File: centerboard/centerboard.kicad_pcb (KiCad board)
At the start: 2 copper layers, 71 parts, among them U1 ATmega32U4-A

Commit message: centerboard messing around
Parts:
- removed D1, D10, D11, D12, D13, D14, D15, D16, D17, D18, D19, D2, D20, D21, D22, D23, D24, D25, D26, D27, D28, D29, D3, D30, D31, D32, D33, D34, D35, D36, D37, D38, D39, D4, D40, D41, D42, D43, D44, D45, D46, D47, D48, D49, D5, D50, D51, D52, D53, D54, D55, D56, D6, D7, D8, D9: 1N4148W, Diode_SMD:D_SOD-123
- removed JC_LA1, JC_LB1, JC_LC1, JC_LD1, JC_LE1, JC_LF1, JC_LT1, JC_RA1, JC_RB1, JC_RC1, JC_RD1, JC_RE1, JC_RF1, JC_RT1: Conn_01x05_MountingPin, Connector_FFC-FPC:TE_84952-5_1x05-1MP_P1.0mm_Horizontal
- added J1: Conn_02x05_Odd_Even, Connector_IDC:IDC-Header_2x05_P2.54mm_Vertical, F.Cu at (96.5, 137.5)
- added J2: USB_B_Micro, Connector_USB:USB_Micro-B_Molex-105017-0001, F.Cu at (101.7, 49.5)
- added JC_L1: Conn_01x05_MountingPin, Connector_FFC-FPC:TE_84952-5_1x05-1MP_P1.0mm_Horizontal, F.Cu at (114.0, 82.2)
- added JC_L2: Conn_01x05_MountingPin, Connector_FFC-FPC:TE_84952-5_1x05-1MP_P1.0mm_Horizontal, F.Cu at (125.8, 85.0)
- added JC_L3: Conn_01x05_MountingPin, Connector_FFC-FPC:TE_84952-5_1x05-1MP_P1.0mm_Horizontal, F.Cu at (125.8, 101.0)
- added JC_L4: Conn_01x05_MountingPin, Connector_FFC-FPC:TE_84952-5_1x05-1MP_P1.0mm_Horizontal, F.Cu at (125.8, 117.0)
- added JC_L5: Conn_01x05_MountingPin, Connector_FFC-FPC:TE_84952-5_1x05-1MP_P1.0mm_Horizontal, F.Cu at (125.8, 133.0)
- added JC_L6: Conn_01x05_MountingPin, Connector_FFC-FPC:TE_84952-5_1x05-1MP_P1.0mm_Horizontal, F.Cu at (125.8, 149.0)
- added JC_L7: Conn_01x05_MountingPin, Connector_FFC-FPC:TE_84952-5_1x05-1MP_P1.0mm_Horizontal, F.Cu at (114.0, 151.8)
- added JC_R1: Conn_01x05_MountingPin, Connector_FFC-FPC:TE_84952-5_1x05-1MP_P1.0mm_Horizontal, F.Cu at (88.0, 82.2)
- added JC_R2: Conn_01x05_MountingPin, Connector_FFC-FPC:TE_84952-5_1x05-1MP_P1.0mm_Horizontal, F.Cu at (76.2, 85.0)
- added JC_R3: Conn_01x05_MountingPin, Connector_FFC-FPC:TE_84952-5_1x05-1MP_P1.0mm_Horizontal, F.Cu at (76.2, 101.0)
- added JC_R4: Conn_01x05_MountingPin, Connector_FFC-FPC:TE_84952-5_1x05-1MP_P1.0mm_Horizontal, F.Cu at (76.2, 117.0)
- added JC_R5: Conn_01x05_MountingPin, Connector_FFC-FPC:TE_84952-5_1x05-1MP_P1.0mm_Horizontal, F.Cu at (76.2, 133.0)
- added JC_R6: Conn_01x05_MountingPin, Connector_FFC-FPC:TE_84952-5_1x05-1MP_P1.0mm_Horizontal, F.Cu at (76.2, 149.0)
- added JC_R7: Conn_01x05_MountingPin, Connector_FFC-FPC:TE_84952-5_1x05-1MP_P1.0mm_Horizontal, F.Cu at (88.0, 151.8)
- added SW1: SW_Push, Button_Switch_SMD:SW_Push_SPST_NO_Alps_SKRK, F.Cu at (106.1, 133.0)
- moved U1 47.8 mm to (102.0, 103.0)
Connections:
- net Net-(U1-GND-Pad15) renamed GND
- net Net-(U1-VCC-Pad14) renamed VCC
- U1 pad 10: COL_RC -> MOSI
- U1 pad 11: COL_RD -> MISO
- U1 pad 12: COL_LA -> unconnected-(U1-PB7-Pad12)
- U1 pad 13: unconnected-(U1-~{RESET}-Pad13) -> RST
- U1 pad 18: COL_LD -> unconnected-(U1-PD0-Pad18)
- U1 pad 19: COL_LE -> unconnected-(U1-PD1-Pad19)
- U1 pad 20: COL_LF -> unconnected-(U1-PD2-Pad20)
- U1 pad 21: COL_LT -> unconnected-(U1-PD3-Pad21)
- U1 pad 22: ROW_2 -> unconnected-(U1-PD5-Pad22)
- U1 pad 25: ROW_1 -> unconnected-(U1-PD4-Pad25)
- U1 pad 26: ROW_3 -> unconnected-(U1-PD6-Pad26)
- U1 pad 27: ROW_4 -> unconnected-(U1-PD7-Pad27)
- U1 pad 28: COL_RE -> unconnected-(U1-PB4-Pad28)
- U1 pad 29: COL_RF -> unconnected-(U1-PB5-Pad29)
- U1 pad 3: unconnected-(U1-D--Pad3) -> Net-(J2-D-)
- U1 pad 30: COL_RT -> unconnected-(U1-PB6-Pad30)
- U1 pad 31: COL_LB -> unconnected-(U1-PC6-Pad31)
- U1 pad 32: COL_LC -> unconnected-(U1-PC7-Pad32)
- U1 pad 4: unconnected-(U1-D+-Pad4) -> Net-(J2-D+)
- U1 pad 8: COL_RA -> unconnected-(U1-PB0-Pad8)
- U1 pad 9: COL_RB -> SCK

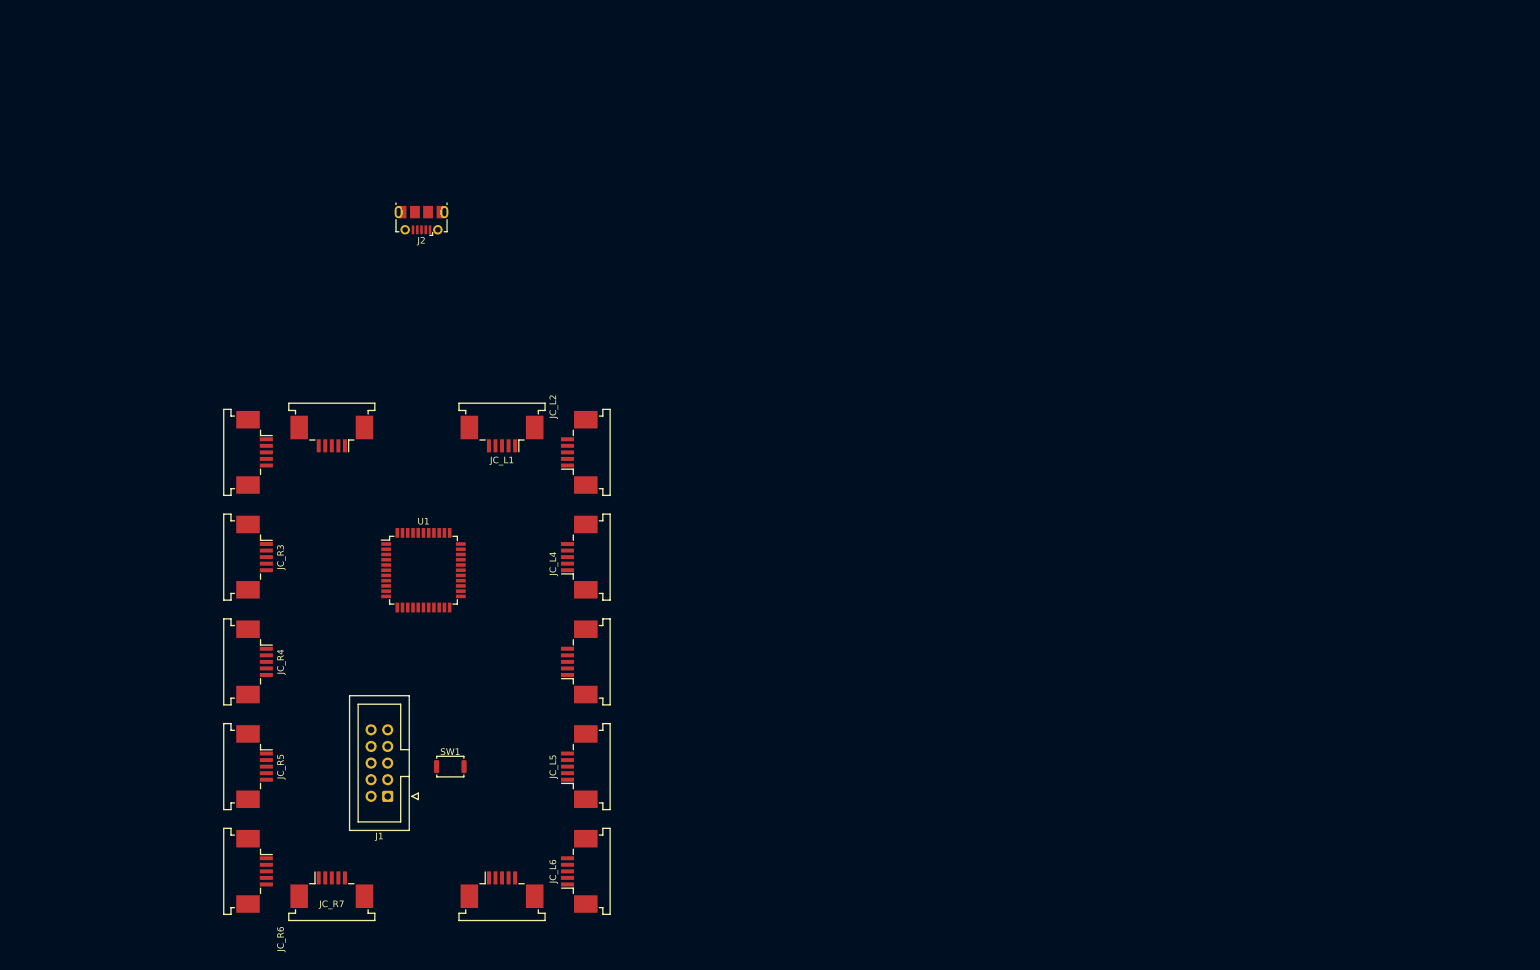
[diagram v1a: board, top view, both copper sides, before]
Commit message: Various tweaks. About to flip centerboard, not feeling too confident in the results there
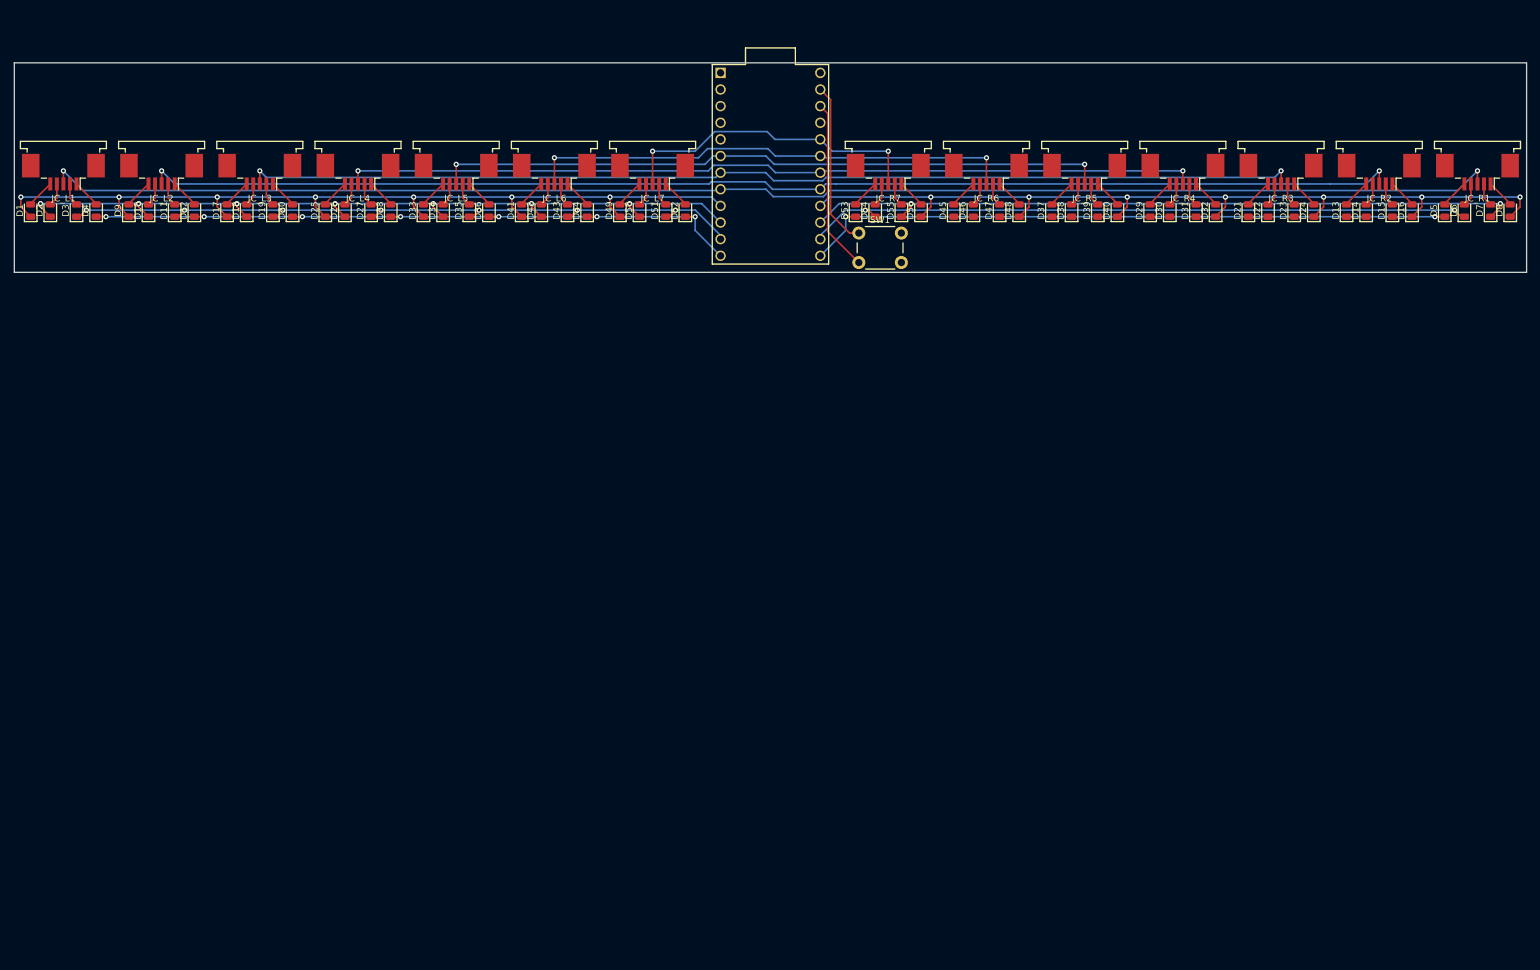
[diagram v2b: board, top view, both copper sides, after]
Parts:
- removed J1: Conn_02x05_Odd_Even, Connector_IDC:IDC-Header_2x05_P2.54mm_Vertical
- removed J2: USB_B_Micro, Connector_USB:USB_Micro-B_Molex-105017-0001
- added D1: 1N4148W, Diode_SMD:D_0805_2012Metric, F.Cu at (42.0, 48.1)
- added D10: 1N4148W, Diode_SMD:D_0805_2012Metric, F.Cu at (60.0, 48.1)
- added D11: 1N4148W, Diode_SMD:D_0805_2012Metric, F.Cu at (64.0, 48.1)
- added D12: 1N4148W, Diode_SMD:D_0805_2012Metric, F.Cu at (67.0, 48.1)
- added D13: 1N4148W, Diode_SMD:D_0805_2012Metric, F.Cu at (243.0, 48.1)
- added D14: 1N4148W, Diode_SMD:D_0805_2012Metric, F.Cu at (246.0, 48.1)
- added D15: 1N4148W, Diode_SMD:D_0805_2012Metric, F.Cu at (250.0, 48.1)
- added D16: 1N4148W, Diode_SMD:D_0805_2012Metric, F.Cu at (253.0, 48.1)
- added D17: 1N4148W, Diode_SMD:D_0805_2012Metric, F.Cu at (72.0, 48.1)
- added D18: 1N4148W, Diode_SMD:D_0805_2012Metric, F.Cu at (75.0, 48.1)
- added D19: 1N4148W, Diode_SMD:D_0805_2012Metric, F.Cu at (79.0, 48.1)
- added D2: 1N4148W, Diode_SMD:D_0805_2012Metric, F.Cu at (45.0, 48.1)
- added D20: 1N4148W, Diode_SMD:D_0805_2012Metric, F.Cu at (82.0, 48.1)
- added D21: 1N4148W, Diode_SMD:D_0805_2012Metric, F.Cu at (228.0, 48.1)
- added D22: 1N4148W, Diode_SMD:D_0805_2012Metric, F.Cu at (231.0, 48.1)
- added D23: 1N4148W, Diode_SMD:D_0805_2012Metric, F.Cu at (235.0, 48.1)
- added D24: 1N4148W, Diode_SMD:D_0805_2012Metric, F.Cu at (238.0, 48.1)
- added D25: 1N4148W, Diode_SMD:D_0805_2012Metric, F.Cu at (87.0, 48.1)
- added D26: 1N4148W, Diode_SMD:D_0805_2012Metric, F.Cu at (90.0, 48.1)
- added D27: 1N4148W, Diode_SMD:D_0805_2012Metric, F.Cu at (94.0, 48.1)
- added D28: 1N4148W, Diode_SMD:D_0805_2012Metric, F.Cu at (97.0, 48.1)
- added D29: 1N4148W, Diode_SMD:D_0805_2012Metric, F.Cu at (213.0, 48.1)
- added D3: 1N4148W, Diode_SMD:D_0805_2012Metric, F.Cu at (49.0, 48.1)
- added D30: 1N4148W, Diode_SMD:D_0805_2012Metric, F.Cu at (216.0, 48.1)
- added D31: 1N4148W, Diode_SMD:D_0805_2012Metric, F.Cu at (220.0, 48.1)
- added D32: 1N4148W, Diode_SMD:D_0805_2012Metric, F.Cu at (223.0, 48.1)
- added D33: 1N4148W, Diode_SMD:D_0805_2012Metric, F.Cu at (102.0, 48.1)
- added D34: 1N4148W, Diode_SMD:D_0805_2012Metric, F.Cu at (105.0, 48.1)
- added D35: 1N4148W, Diode_SMD:D_0805_2012Metric, F.Cu at (109.0, 48.1)
- added D36: 1N4148W, Diode_SMD:D_0805_2012Metric, F.Cu at (112.0, 48.1)
- added D37: 1N4148W, Diode_SMD:D_0805_2012Metric, F.Cu at (198.0, 48.1)
- added D38: 1N4148W, Diode_SMD:D_0805_2012Metric, F.Cu at (201.0, 48.1)
- added D39: 1N4148W, Diode_SMD:D_0805_2012Metric, F.Cu at (205.0, 48.1)
- added D4: 1N4148W, Diode_SMD:D_0805_2012Metric, F.Cu at (52.0, 48.1)
- added D40: 1N4148W, Diode_SMD:D_0805_2012Metric, F.Cu at (208.0, 48.1)
- added D41: 1N4148W, Diode_SMD:D_0805_2012Metric, F.Cu at (117.0, 48.1)
- added D42: 1N4148W, Diode_SMD:D_0805_2012Metric, F.Cu at (120.0, 48.1)
- added D43: 1N4148W, Diode_SMD:D_0805_2012Metric, F.Cu at (124.0, 48.1)
- added D44: 1N4148W, Diode_SMD:D_0805_2012Metric, F.Cu at (127.0, 48.1)
- added D45: 1N4148W, Diode_SMD:D_0805_2012Metric, F.Cu at (183.0, 48.1)
- added D46: 1N4148W, Diode_SMD:D_0805_2012Metric, F.Cu at (186.0, 48.1)
- added D47: 1N4148W, Diode_SMD:D_0805_2012Metric, F.Cu at (190.0, 48.1)
- added D48: 1N4148W, Diode_SMD:D_0805_2012Metric, F.Cu at (193.0, 48.1)
- added D49: 1N4148W, Diode_SMD:D_0805_2012Metric, F.Cu at (132.0, 48.1)
- added D5: 1N4148W, Diode_SMD:D_0805_2012Metric, F.Cu at (258.0, 48.1)
- added D50: 1N4148W, Diode_SMD:D_0805_2012Metric, F.Cu at (135.0, 48.1)
- added D51: 1N4148W, Diode_SMD:D_0805_2012Metric, F.Cu at (139.0, 48.1)
- added D52: 1N4148W, Diode_SMD:D_0805_2012Metric, F.Cu at (142.0, 48.1)
- added D53: 1N4148W, Diode_SMD:D_0805_2012Metric, F.Cu at (168.0, 48.1)
- added D54: 1N4148W, Diode_SMD:D_0805_2012Metric, F.Cu at (171.0, 48.1)
- added D55: 1N4148W, Diode_SMD:D_0805_2012Metric, F.Cu at (175.0, 48.1)
- added D56: 1N4148W, Diode_SMD:D_0805_2012Metric, F.Cu at (178.0, 48.1)
- added D6: 1N4148W, Diode_SMD:D_0805_2012Metric, F.Cu at (261.0, 48.1)
- added D7: 1N4148W, Diode_SMD:D_0805_2012Metric, F.Cu at (265.0, 48.1)
- added D8: 1N4148W, Diode_SMD:D_0805_2012Metric, F.Cu at (268.0, 48.1)
- added D9: 1N4148W, Diode_SMD:D_0805_2012Metric, F.Cu at (57.0, 48.1)
- SW1: footprint Button_Switch_SMD:SW_Push_SPST_NO_Alps_SKRK -> Button_Switch_THT:SW_PUSH_6mm
- U1: value ATmega32U4-A -> ProMicro; footprint Package_QFP:TQFP-44_10x10mm_P0.8mm -> promicro:ProMicro
- moved JC_R1 179.5 mm to (263.0, 42.2)
- moved JC_R2 177.1 mm to (248.0, 42.2), turned to 180 degrees
- moved JC_R3 167.5 mm to (233.0, 42.2), turned to 180 degrees
- moved JC_R4 160.3 mm to (218.0, 42.2), turned to 180 degrees
- moved JC_R5 156.0 mm to (203.0, 42.2), turned to 180 degrees
- moved JC_R6 154.6 mm to (188.0, 42.2), turned to 180 degrees
- moved JC_R7 138.7 mm to (173.0, 42.2), turned to 180 degrees
- moved JC_L7 112.0 mm to (137.0, 42.2), turned to 180 degrees
- moved JC_L6 106.9 mm to (122.0, 42.2), turned to 180 degrees
- moved SW1 102.6 mm to (168.5, 51.5)
- moved JC_L5 92.7 mm to (107.0, 42.2), turned to 180 degrees
- moved JC_L4 82.1 mm to (92.0, 42.2), turned to 180 degrees
- moved U1 81.6 mm to (155.0, 41.0), turned to -90 degrees
- moved JC_L1 78.0 mm to (47.0, 42.2)
- moved JC_L2 76.8 mm to (62.0, 42.2), turned to 180 degrees
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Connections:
- SW1 pad 1: RST -> Net-(SW1-Pad1)
- SW1 pad 2: GND -> Net-(U1-RST)
- U1 pad 10: MOSI -> ROW_L2
- U1 pad 11: MISO -> ROW_L3
- U1 pad 12: unconnected-(U1-PB7-Pad12) -> ROW_L4
- U1 pad 13: RST -> ROW_R1
- U1 pad 14: VCC -> ROW_R2
- U1 pad 15: GND -> ROW_R3
- U1 pad 16: unconnected-(U1-XTAL2-Pad16) -> ROW_R4
- U1 pad 17: unconnected-(U1-XTAL1-Pad17) -> COL_2
- U1 pad 18: unconnected-(U1-PD0-Pad18) -> COL_4
- U1 pad 19: unconnected-(U1-PD1-Pad19) -> COL_6
- U1 pad 20: unconnected-(U1-PD2-Pad20) -> COL_7
- U1 pad 22: unconnected-(U1-PD5-Pad22) -> Net-(U1-RST)
- U1 pad 23: GND -> Net-(SW1-Pad1)
- U1 pad 24: Net-(U1-AVCC-Pad24) -> unconnected-(U1-RAW-Pad24)
- U1 pad 3: Net-(J2-D-) -> unconnected-(U1-GND-Pad3)
- U1 pad 4: Net-(J2-D+) -> unconnected-(U1-GND-Pad4)
- U1 pad 6: unconnected-(U1-UCAP-Pad6) -> COL_5
- U1 pad 7: unconnected-(U1-VBUS-Pad7) -> COL_3
- U1 pad 8: unconnected-(U1-PB0-Pad8) -> COL_1
- U1 pad 9: SCK -> ROW_L1
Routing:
- net COL_1: track 0.00 -> 223.1 mm, vias 0 -> 2
- net COL_2: track 0.00 -> 192.6 mm, vias 0 -> 2
- net COL_3: track 0.00 -> 161.8 mm, vias 0 -> 2
- net ROW_R4: track 0.00 -> 132.8 mm, vias 0 -> 7
- net ROW_L1: track 0.00 -> 132.8 mm, vias 0 -> 7
- net COL_4: track 0.00 -> 130.9 mm, vias 0 -> 2
- net ROW_L2: track 0.00 -> 123.4 mm, vias 0 -> 7
- net ROW_L3: track 0.00 -> 113.0 mm, vias 0 -> 7
- net ROW_R3: track 0.00 -> 110.3 mm, vias 0 -> 2
- net ROW_L4: track 0.00 -> 108.1 mm, vias 0 -> 7
- net COL_5: track 0.00 -> 103.1 mm, vias 0 -> 2
- net ROW_R2: track 0.00 -> 102.9 mm, vias 0 -> 2
- net ROW_R1: track 0.00 -> 100.6 mm, vias 0 -> 2
- net COL_6: track 0.00 -> 75.2 mm, vias 0 -> 2
- net COL_7: track 0.00 -> 48.5 mm, vias 0 -> 2
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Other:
- board outline added: 231 x 32 mm

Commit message: misc tidying
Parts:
- D1, D2, D3, D37, D38, D39, D4, D40, JC_L1, JC_L2, JC_L3, JC_L4, JC_L5, JC_L6, JC_L7, JC_R1, JC_R2, JC_R3, JC_R4, JC_R5, JC_R6, JC_R7, SW1, U1: moved to B.Cu
- D10: renamed from D18; moved to B.Cu
- D11: renamed from D19; moved to B.Cu
- D12: renamed from D20; moved to B.Cu
- D13: renamed from D25; moved to B.Cu
- D14: renamed from D26; moved to B.Cu
- D15: renamed from D27; moved to B.Cu
- D16: renamed from D28; moved to B.Cu
- D17: renamed from D33; moved to B.Cu
- D18: renamed from D34; moved to B.Cu
- D19: renamed from D35; moved to B.Cu
- D20: renamed from D36; moved to B.Cu
- D21: renamed from D41; moved to B.Cu
- D22: renamed from D42; moved to B.Cu
- D23: renamed from D43; moved to B.Cu
- D24: renamed from D44; moved to B.Cu
- D25: renamed from D49; moved to B.Cu
- D26: renamed from D50; moved to B.Cu
- D27: renamed from D51; moved to B.Cu
- D28: renamed from D52; moved to B.Cu
- D29: renamed from D53; moved to B.Cu
- D30: renamed from D54; moved to B.Cu
- D31: renamed from D55; moved to B.Cu
- D32: renamed from D56; moved to B.Cu
- D33: renamed from D45; moved to B.Cu
- D34: renamed from D46; moved to B.Cu
- D35: renamed from D47; moved to B.Cu
- D36: renamed from D48; moved to B.Cu
- D41: renamed from D29; moved to B.Cu
- D42: renamed from D30; moved to B.Cu
- D43: renamed from D31; moved to B.Cu
- D44: renamed from D32; moved to B.Cu
- D45: renamed from D21; moved to B.Cu
- D46: renamed from D22; moved to B.Cu
- D47: renamed from D23; moved to B.Cu
- D48: renamed from D24; moved to B.Cu
- D49: renamed from D13; moved to B.Cu
- D5: renamed from D9; moved to B.Cu
- D50: renamed from D14; moved to B.Cu
- D51: renamed from D15; moved to B.Cu
- D52: renamed from D16; moved to B.Cu
- D53: renamed from D5; moved to B.Cu
- D54: renamed from D6; moved to B.Cu
- D55: renamed from D7; moved to B.Cu
- D56: renamed from D8; moved to B.Cu
- D6: renamed from D10; moved to B.Cu
- D7: renamed from D11; moved to B.Cu
- D8: renamed from D12; moved to B.Cu
- D9: renamed from D17; moved to B.Cu
- moved D1 226.0 mm to (268.0, 48.1)
- moved D56 226.0 mm to (42.0, 48.1)
- moved D2 220.0 mm to (265.0, 48.1)
- moved D55 220.0 mm to (45.0, 48.1)
- moved JC_L1 216.0 mm to (263.0, 42.2), turned to 0 degrees
- moved JC_R1 216.0 mm to (47.0, 42.2), turned to 0 degrees
- moved D3 212.0 mm to (261.0, 48.1)
- moved D54 212.0 mm to (49.0, 48.1)
- moved D4 206.0 mm to (258.0, 48.1)
- moved D53 206.0 mm to (52.0, 48.1)
- moved D5 196.0 mm to (253.0, 48.1)
- moved D52 196.0 mm to (57.0, 48.1)
- moved D51 190.0 mm to (60.0, 48.1)
- moved D6 190.0 mm to (250.0, 48.1)
- moved JC_L2 186.0 mm to (248.0, 42.2), turned to 0 degrees
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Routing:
- net ROW_R3: track 110.3 -> 123.4 mm, vias 2 -> 7
- net unconnected-(JC_R7-MountPin-PadMP): track 0.00 -> 12.4 mm
- net unconnected-(JC_L7-MountPin-PadMP): track 0.00 -> 12.4 mm
- net unconnected-(JC_L6-MountPin-PadMP): track 0.00 -> 11.6 mm
- net unconnected-(JC_R6-MountPin-PadMP): track 0.00 -> 11.6 mm
- net unconnected-(JC_L4-MountPin-PadMP): track 0.00 -> 9.98 mm
- net unconnected-(JC_L3-MountPin-PadMP): track 0.00 -> 9.98 mm
- net unconnected-(JC_L2-MountPin-PadMP): track 0.00 -> 9.98 mm
- net unconnected-(JC_L1-MountPin-PadMP): track 0.00 -> 9.98 mm
- net unconnected-(JC_R1-MountPin-PadMP): track 0.00 -> 9.98 mm
- net unconnected-(JC_R2-MountPin-PadMP): track 0.00 -> 9.98 mm
- net unconnected-(JC_R4-MountPin-PadMP): track 0.00 -> 9.98 mm
- net unconnected-(JC_R3-MountPin-PadMP): track 0.00 -> 9.98 mm
- net unconnected-(JC_R5-MountPin-PadMP): track 0.00 -> 8.13 mm
- net unconnected-(JC_L5-MountPin-PadMP): track 0.00 -> 8.13 mm
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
